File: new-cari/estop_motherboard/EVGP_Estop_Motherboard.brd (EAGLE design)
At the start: 82.6 x 94.1 mm, 45 parts, among them J1 JST-XH-02-PIN-LONG-PAD, J2 JST-XH-02-PIN-LONG-PAD, J3 JST-XH-03-PIN-LONG-PAD, J4 JST-XH-03-PIN-LONG-PAD, J5 AVR_SPI_PROG_3X2PTH, J6 UX60-MB-5S8, J7 JST-XH-04-PIN-LONG-PAD, J8 JST-XH-03-PIN-LONG-PAD, J9 JST-XH-02-PIN-LONG-PAD, Q1 NFETS_1, Q2 N_FETS2, U1 ATMEGA32U4-AU, U2 NL27WZ08USG, U3 NL27WZ08USG, X1 TSX-3225 16.0000MF18X-AC0

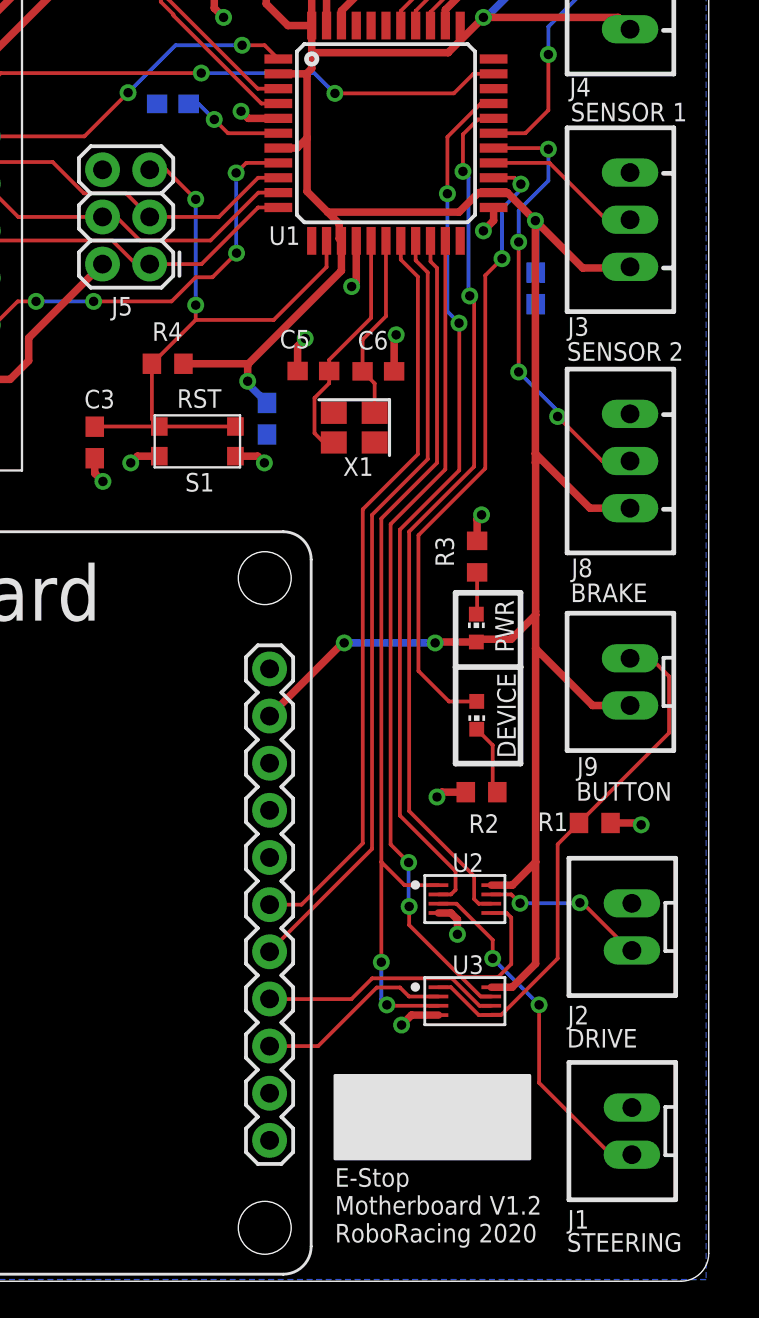
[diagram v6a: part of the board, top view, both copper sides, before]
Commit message: Fixed flipped pins on gates and mosfets, added details on schematic
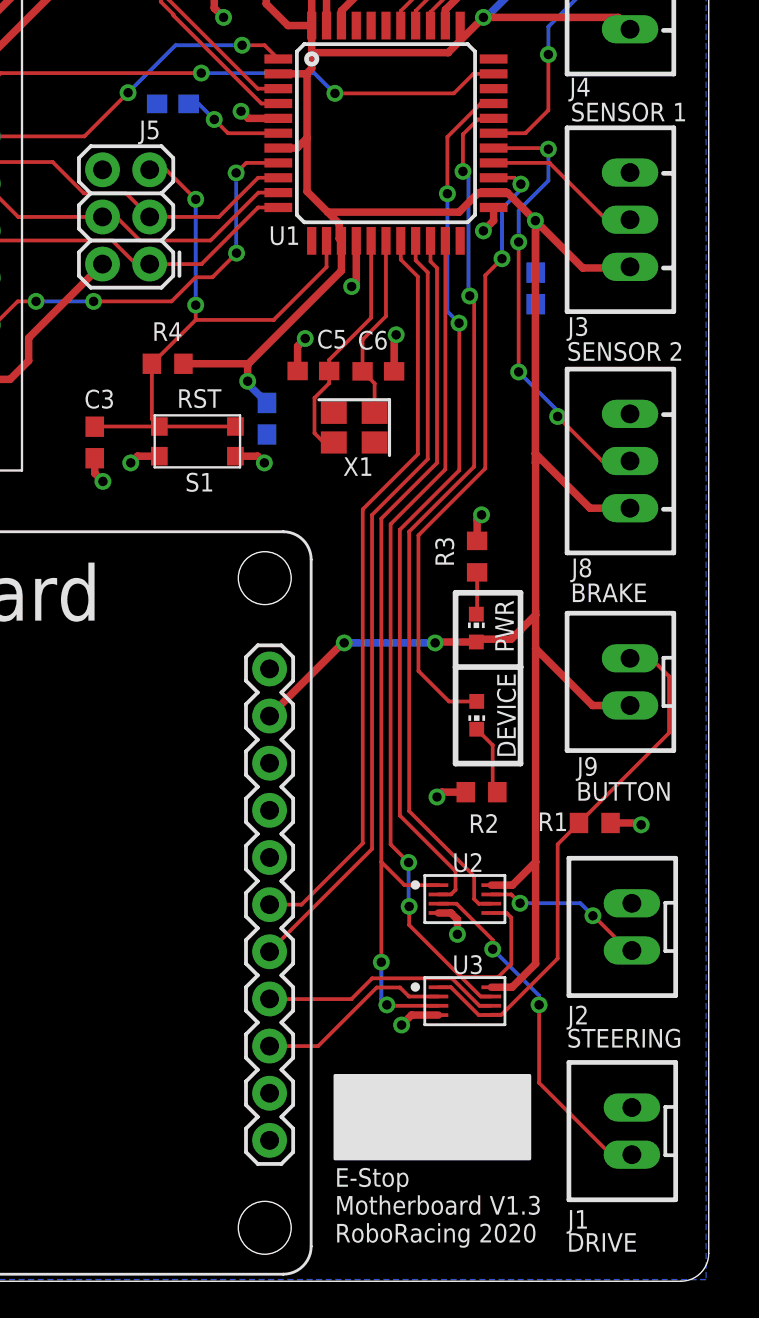
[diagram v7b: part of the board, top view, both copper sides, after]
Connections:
- net DRIVE_EN_OUT: now also J1.1, U2.3; no longer J2.1, U2.7
- net STACK_CON1: now also J7.3, Q2.3; no longer J7.2, Q2.6
- net STACK_CON2: now also J7.2, Q2.6; no longer J7.3, Q2.3
- net STEERING_EN_OUT: now also J2.1, U2.7; no longer J1.1, U2.3
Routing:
- net STEERING_EN_OUT: track 19.1 -> 8.83 mm
- net DRIVE_EN_OUT: track 8.86 -> 19.1 mm
- net STACK_CON2: track 9.40 -> 7.49 mm
- net STACK_CON1: track 7.49 -> 9.40 mm
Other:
- board text added: "E-Stop Motherboard V1.3 RoboRacing 2020"
- board text removed: "E-Stop Motherboard V1.2 RoboRacing 2020"
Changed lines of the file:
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@@
 <?xml version="1.0" encoding="utf-8"?>
 <!DOCTYPE eagle SYSTEM "eagle.dtd">
-<eagle version="9.5.1">
+<eagle version="9.5.0">
 <drawing>
 <settings>
@@
 <text x="67.5" y="75.8" size="1" layer="21" font="vector">0.5A</text>
 <text x="68.5" y="-3.5" size="1" layer="21" font="vector">E-Stop
-Motherboard V1.2
+Motherboard V1.3
 RoboRacing 2020</text>
 <polygon width="0.1524" layer="21">
@@
 </polygon>
 <hole x="84" y="84" drill="3.3"/>
-<text x="81" y="-4" size="1" layer="25" font="vector">STEERING</text>
-<text x="81" y="7" size="1" layer="25" font="vector">DRIVE</text>
+<text x="81" y="-4" size="1" layer="25" font="vector">DRIVE</text>
+<text x="81" y="7" size="1" layer="25" font="vector">STEERING</text>
 <text x="81.2" y="31" size="1" layer="25" font="vector">BRAKE</text>
 <text x="81" y="44" size="1" layer="25" font="vector">SENSOR 2</text>
@@
 </element>
 <element name="C5" library="resistor" library_urn="urn:adsk.eagle:library:348" package="C0603" package3d_urn="urn:adsk.eagle:package:23616/2" value="9pF" x="67.34" y="43.45" smashed="yes" rot="R180">
-<attribute name="NAME" x="65.525" y="44.665" size="1" layer="25" font="vector"/>
+<attribute name="NAME" x="67.525" y="44.665" size="1" layer="25" font="vector"/>
 </element>
 <element name="C1" library="rcl" library_urn="urn:adsk.eagle:library:334" package="C1206" package3d_urn="urn:adsk.eagle:package:23618/2" value="47uF" x="63.4" y="64.67" smashed="yes">
@@
 <element name="RADIO" library="board_outline" package="RADIO_V1.3" value="E-STOP HEADER" x="7.22" y="-5.21" smashed="yes"/>
 <element name="J5" library="SparkFun-Connectors" library_urn="urn:adsk.eagle:library:513" package="2X3" package3d_urn="urn:adsk.eagle:package:38016/1" value="AVR_SPI_PROG_3X2PTH" x="58.52" y="49.21" smashed="yes" rot="R90">
-<attribute name="NAME" x="56.456" y="46.44" size="1" layer="25" font="vector"/>
+<attribute name="NAME" x="57.956" y="55.94" size="1" layer="25" font="vector"/>
 </element>
 <element name="J6" library="RoboJackets-Connectors" package="UX60-MB-5S8" value="UX60-MB-5S8" x="58.7" y="88.49" smashed="yes" rot="R270">
@@
 <wire x1="64.71" y1="61" x2="65.45" y2="60.26" width="0.2032" layer="1"/>
 </signal>
-<signal name="STACK_CON1">
+<signal name="STACK_CON2">
 <contactref element="Q2" pad="6"/>
 <contactref element="J7" pad="2"/>
@@
 <wire x1="68.49" y1="80.31788125" x2="68.49" y2="84.8" width="0.2032" layer="1"/>
 </signal>
-<signal name="STACK_CON2">
+<signal name="STACK_CON1">
 <contactref element="Q2" pad="3"/>
 <contactref element="J7" pad="3"/>
@@
 <wire x1="85.53" y1="27.97" x2="84.4" y2="27.97" width="0.2032" layer="1"/>
 </signal>
-<signal name="DRIVE_EN_OUT">
+<signal name="STEERING_EN_OUT">
 <contactref element="U2" pad="7"/>
 <contactref element="J2" pad="1"/>
-<wire x1="84.5" y1="12.23" x2="84.4" y2="12.23" width="0.2032" layer="1"/>
-<wire x1="84.4" y1="12.23" x2="81.83" y2="14.8" width="0.2032" layer="1"/>
-<wire x1="81.7" y1="14.8" x2="81.83" y2="14.8" width="0.2032" layer="1"/>
+<wire x1="84.5" y1="12.23" x2="84.3" y2="12.23" width="0.2032" layer="1"/>
+<wire x1="84.3" y1="12.23" x2="82.43" y2="14.1" width="0.2032" layer="1"/>
+<wire x1="82.4" y1="14.1" x2="82.43" y2="14.1" width="0.2032" layer="1"/>
 <wire x1="76.9224" y1="15.25" x2="78.0008" y2="15.25" width="0.2032" layer="1"/>
 <wire x1="78.0008" y1="15.25" x2="78.4744" y2="14.7764" width="0.2032" layer="1"/>
 <via x="78.4744" y="14.7764" extent="1-16" drill="0.508"/>
-<wire x1="78.4744" y1="14.7764" x2="81.7" y2="14.7764" width="0.2032" layer="16"/>
-<wire x1="81.7" y1="14.7764" x2="81.7" y2="14.8" width="0.2032" layer="16"/>
-<via x="81.7" y="14.8" extent="1-16" drill="0.508"/>
+<wire x1="78.4744" y1="14.7764" x2="81.7236" y2="14.7764" width="0.2032" layer="16"/>
+<wire x1="81.7236" y1="14.7764" x2="82.4" y2="14.1" width="0.2032" layer="16"/>
+<via x="82.4" y="14.1" extent="1-16" drill="0.508"/>
 </signal>
 <signal name="START_RB">
@@
 <wire x1="72.969" y1="38.969" x2="70" y2="36" width="0.2032" layer="1"/>
 </signal>
-<signal name="STEERING_EN_OUT">
+<signal name="DRIVE_EN_OUT">
 <contactref element="U2" pad="3"/>
 <contactref element="J1" pad="1"/>
 <wire x1="74.0776" y1="14.75" x2="75.05" y2="14.75" width="0.2032" layer="1"/>
-<wire x1="77" y1="12.8" x2="77" y2="11.8" width="0.2032" layer="1"/>
-<via x="77" y="11.8" extent="1-16" drill="0.508"/>
-<wire x1="77" y1="11.8" x2="79.5" y2="9.3" width="0.2032" layer="16"/>
+<wire x1="77" y1="12.8" x2="77" y2="12.3" width="0.2032" layer="1"/>
+<via x="77" y="12.3" extent="1-16" drill="0.508"/>
+<wire x1="79.5" y1="9.8" x2="79.5" y2="9.3" width="0.2032" layer="16"/>
+<wire x1="79.5" y1="9.8" x2="77" y2="12.3" width="0.2032" layer="16"/>
 <via x="79.5" y="9.3" extent="1-16" drill="0.508"/>
 <wire x1="84.5" y1="1.23" x2="83.37" y2="1.23" width="0.2032" layer="1"/>

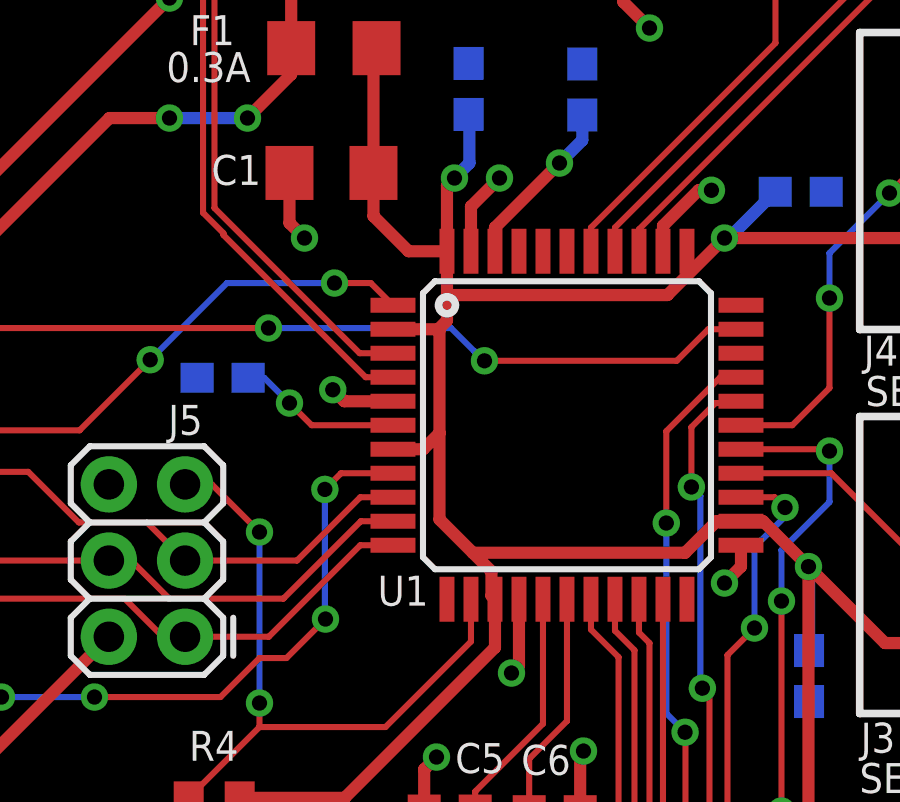
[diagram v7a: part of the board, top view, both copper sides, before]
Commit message: Updated SS pin and trace
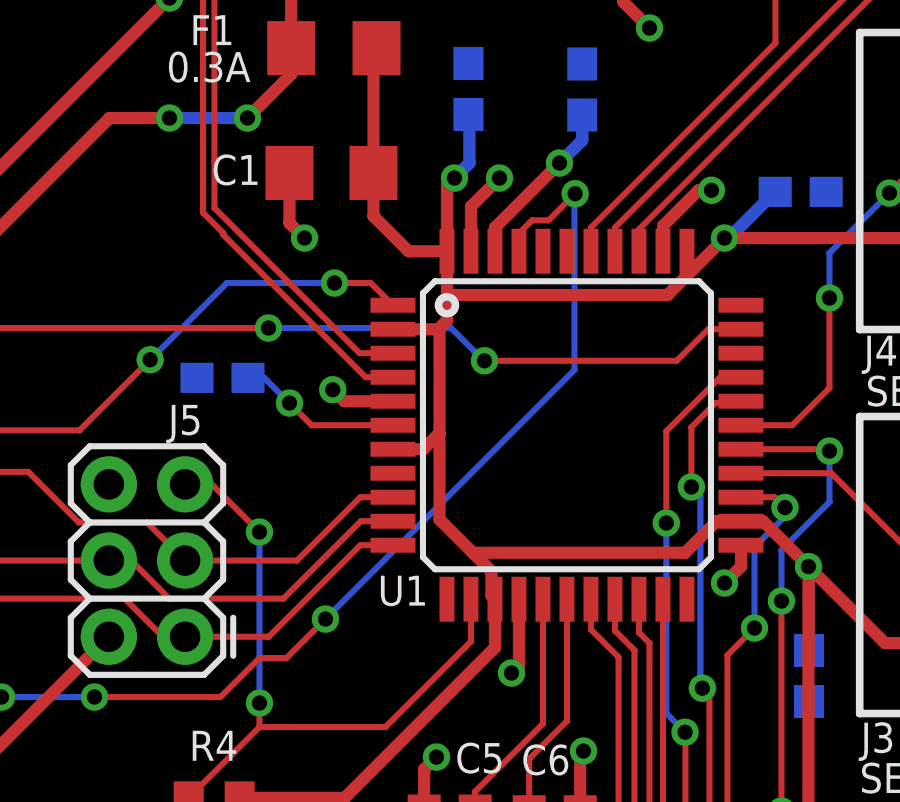
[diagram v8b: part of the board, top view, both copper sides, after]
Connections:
- net SS: now also U1.41; no longer U1.8
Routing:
- net SS: track 22.0 -> 35.8 mm
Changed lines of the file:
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@@
 <?xml version="1.0" encoding="utf-8"?>
 <!DOCTYPE eagle SYSTEM "eagle.dtd">
-<eagle version="9.5.0">
+<eagle version="9.5.1">
 <drawing>
 <settings>
@@
 <signal name="SS">
 <contactref element="U$2" pad="6"/>
-<contactref element="U1" pad="8"/>
 <wire x1="51.41" y1="47.2" x2="50.14" y2="45.93" width="0.2032" layer="1"/>
 <wire x1="49.64" y1="45.93" x2="50.14" y2="45.93" width="0.2032" layer="1"/>
@@
 <wire x1="55.5" y1="47.2" x2="52.4" y2="47.2" width="0.2032" layer="16"/>
 <via x="55.5" y="47.2" extent="1-16" drill="0.508"/>
-<via x="63.17914375" y="54.12085625" extent="1-16" drill="0.508"/>
-<wire x1="63.17914375" y1="54.12085625" x2="63.7182875" y2="54.66" width="0.2032" layer="1"/>
-<wire x1="63.7182875" y1="54.66" x2="65.45" y2="54.66" width="0.2032" layer="1"/>
 <wire x1="59.7" y1="47.2" x2="61" y2="48.5" width="0.2032" layer="1"/>
 <wire x1="61" y1="48.5" x2="61.9" y2="48.5" width="0.2032" layer="1"/>
 <wire x1="61.9" y1="48.5" x2="63.2" y2="49.8" width="0.2032" layer="1"/>
 <via x="63.2" y="49.8" extent="1-16" drill="0.508"/>
-<wire x1="63.2" y1="49.8" x2="63.2" y2="50.1" width="0.2032" layer="16"/>
-<wire x1="63.2" y1="50.1" x2="63.17914375" y2="50.12085625" width="0.2032" layer="16"/>
-<wire x1="63.17914375" y1="50.12085625" x2="63.17914375" y2="54.12085625" width="0.2032" layer="16"/>
 <wire x1="55.5" y1="47.2" x2="59.7" y2="47.2" width="0.2032" layer="1"/>
+<contactref element="U1" pad="41"/>
+<wire x1="63.2" y1="49.8" x2="71.5" y2="58.1" width="0.2032" layer="16"/>
+<wire x1="71.5" y1="63.95539375" x2="71.522303125" y2="63.977696875" width="0.2032" layer="16"/>
+<via x="71.522303125" y="63.977696875" extent="1-16" drill="0.508"/>
+<wire x1="71.522303125" y1="63.977696875" x2="70.63400625" y2="63.0894" width="0.2032" layer="1"/>
+<wire x1="70.63400625" y1="63.0894" x2="70.08426875" y2="63.0894" width="0.2032" layer="1"/>
+<wire x1="70.08426875" y1="63.0894" x2="69.65" y2="62.65513125" width="0.2032" layer="1"/>
+<wire x1="69.65" y1="62.65513125" x2="69.65" y2="62.06" width="0.2032" layer="1"/>
+<wire x1="71.5" y1="58.1" x2="71.5" y2="63.95539375" width="0.2032" layer="16"/>
 </signal>
 <signal name="ETH_RST">
